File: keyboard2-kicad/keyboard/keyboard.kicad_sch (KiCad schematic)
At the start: 232 parts, among them J1 USB_C_Receptacle, J2 USB_BOOT, SW1 Esc, SW10 F9, SW100 Enter, SW11 F10, SW12 F11, SW13 F12, SW14 DEL, SW15 HOME, SW16 END, SW17 PGUP, SW18 PGDN, SW19 INS, SW2 F1, SW20 TILDE, SW21 1, SW22 2, SW23 3, SW24 4, SW25 5, SW26 6, SW27 7, SW28 8, SW29 9, SW3 F2, SW30 0, SW31 -, SW32 =, SW33 BKSP, SW34 Num, SW35 /, SW36 *, SW37 -, SW38 Tab, SW39 Q, SW4 F3, SW40 W, SW41 E, SW42 R, SW43 T, SW44 Y, SW45 U, SW46 I, SW47 O, SW48 P, SW49 [, SW5 F4, SW50 ], SW51 \, SW52 7, SW53 8, SW54 9, SW55 Caps, SW56 A, SW57 S, SW58 D, SW59 F, SW6 F5, SW60 G, SW61 H, SW62 J, SW63 K, SW64 L, SW65 ;, SW66 ", SW67 Enter, SW68 4, SW69 5, SW7 F6, SW70 6, SW71 +, SW72 Shift, SW73 Z, SW74 X, SW75 C, SW76 V, SW77 B, SW78 N, SW79 M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

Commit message: move images and finish schematic
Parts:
- removed J2: USB_BOOT, Connector_PinHeader_2.54mm:PinHeader_1x02_P2.54mm_Vertical, symbol Connector_Generic:Conn_01x02
- added D101, D102, D103, D104, D105, D106, D107, D108, D109, D110, D111, D112, D113, D114, D115, D116, D117, D118, D119, D120, D121, D122, D123, D124, D125, D126, D127, D128, D129, D130, D131, D132, D133, D134, D135, D136, D137, D138, D139, D140, D141, D142, D143, D144, D145, D146, D147, D148, D149, D150, D151, D152, D153, D154, D155, D156, D157, D158, D159, D160, D161, D162, D163, D164, D165, D166, D167, D168, D169, D170, D171, D172, D173, D174, D175, D176, D177, D178, D179, D180, D181, D182, D183, D184, D185, D186, D187, D188, D189, D190, D191, D192, D193, D194, D195, D196, D197, D198, D199, D200: LED, LED_SMD:LED_0603_1608Metric, symbol Device:LED
- added J3: Touchscreen, Connector_PinHeader_2.54mm:PinHeader_1x14_P2.54mm_Vertical, symbol Connector:Conn_01x14_Pin
- added J4: Jack-DC, DC-005:NINIGI_DC-005, symbol Connector:Jack-DC
- added M1, M10, M2, M3, M4, M5, M6, M7, M8, M9: Motor_Servo, Connector_PinHeader_2.54mm:PinHeader_1x03_P2.54mm_Vertical, symbol Motor:Motor_Servo
- added R10, R100, R101, R102, R103, R104, R105, R106, R107, R108, R11, R12, R13, R14, R15, R16, R17, R18, R19, R20, R21, R22, R23, R24, R25, R26, R27, R28, R29, R30, R31, R32, R33, R34, R35, R36, R37, R38, R39, R40, R41, R42, R43, R44, R45, R46, R47, R48, R49, R50, R51, R52, R53, R54, R55, R56, R57, R58, R59, R60, R61, R62, R63, R64, R65, R66, R67, R68, R69, R70, R71, R72, R73, R74, R75, R76, R77, R78, R79, R80, R81, R82, R83, R84, R85, R86, R87, R88, R89, R9, R90, R91, R92, R93, R94, R95, R96, R97, R98, R99: 680R, Resistor_SMD:R_0402_1005Metric, symbol Device:R
- added RV1: Slider 1, PG151101S11:SW_PG151101S11, symbol Device:R_Potentiometer
- added RV2: Slider 2, PG151101S11:SW_PG151101S11, symbol Device:R_Potentiometer
- added S1: USB BOOT, TS-1187A-B-A-B:SW_TS-1187A-B-A-B, symbol TS-1187A-B-A-B:TS-1187A-B-A-B
- added SW101: RotaryEncoder, symbol Device:RotaryEncoder
- added U7: IRLML6344TRPBF, IRLML6344TRPBF:SOT95P240X112-3N, symbol IRLML6344TRPBF:IRLML6344TRPBF
- C12, C13, C14, C3, C4, C5, C6, C7, C8, C9: footprint Capacitor_SMD:C_0603_1608Metric -> Capacitor_SMD:C_0402_1005Metric
- D1, D10, D11, D12, D13, D14, D15, D16, D17, D18, D19, D2, D20, D21, D22, D23, D24, D25, D26, D27, D28, D29, D3, D30, D31, D32, D33, D34, D35, D36, D37, D38, D39, D4, D40, D41, D42, D43, D44, D45, D46, D47, D48, D49, D5, D50, D51, D52, D53, D54, D55, D56, D57, D58, D59, D6, D60, D61, D62, D63, D64, D65, D66, D67, D68, D69, D7, D70, D71, D72, D73, D74, D75, D76, D77, D78, D79, D8, D80, D81, D82, D83, D84, D85, D86, D87, D88, D89, D9, D90, D91, D92, D93, D94, D95, D96, D97, D98, D99: footprint (none) -> Diode_SMD:D_SOD-323
- D100: footprint (none) -> LED_SMD:LED_0603_1608Metric
- J1: footprint (none) -> TYPE-C-31-M-12:HRO_TYPE-C-31-M-12
- R5, R6, R7, R8: footprint (none) -> Resistor_SMD:R_0402_1005Metric
- SW1, SW10, SW100, SW11, SW12, SW13, SW14, SW15, SW16, SW17, SW18, SW19, SW2, SW20, SW21, SW22, SW23, SW24, SW25, SW26, SW27, SW28, SW29, SW3, SW30, SW31, SW32, SW33, SW34, SW35, SW36, SW37, SW38, SW39, SW4, SW40, SW41, SW42, SW43, SW44, SW45, SW46, SW47, SW48, SW49, SW5, SW50, SW51, SW52, SW53, SW54, SW55, SW56, SW57, SW58, SW59, SW6, SW60, SW61, SW62, SW63, SW64, SW65, SW66, SW67, SW68, SW69, SW7, SW70, SW71, SW72, SW73, SW74, SW75, SW76, SW77, SW78, SW79, SW8, SW80, SW81, SW82, SW83, SW84, SW85, SW86, SW87, SW88, SW89, SW9, SW90, SW91, SW92, SW93, SW94, SW95, SW96, SW97, SW98, SW99: footprint (none) -> PG151101S11:SW_PG151101S11
- U3: footprint Package_SO:SOIC-8_5.23x5.23mm_P1.27mm -> W25Q128JVSIQ:SOIC127P790X216-8N
- U4: footprint ABM8-272-T3:ABM8-272-T3 -> ABM8:XTAL_ABM8-272-T3
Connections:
- net +3V3: now also J3.1 (Pin_1), J3.4 (Pin_4), RV1.1, RV2.1
- net GND: now also J3.2 (Pin_2), J4.2, M1.3 (-), M10.3 (-), M2.3 (-), M3.3 (-), M4.3 (-), M5.3 (-), M6.3 (-), M8.3 (-), M9.3 (-), RV1.3, RV2.3, S1.C, S1.D, SW101.C, U7.2 (S)
- net at R2.1: now also S1.A, S1.B
- net SERVO_7: now reaches U1.11 (GPIO8)
- net SERVO_7: now also M7.1 (PWM)
- net SERVO_8: now reaches U1.12 (GPIO9)
- net SERVO_8: now also M8.1 (PWM)
- net SERVO_9: now reaches U1.13 (GPIO10)
- net SERVO_9: now also M9.1 (PWM)
- net SERVO_10: now reaches U1.14 (GPIO11)
- net SERVO_10: now also M10.1 (PWM)
- net EA: now reaches U1.15 (GPIO12)
- net EA: now also SW101.A
- net EB: now reaches U1.16 (GPIO13)
- net EB: now also SW101.B
- net POT_1: now reaches U1.17 (GPIO14)
- net POT_1: now also RV1.2
- net POT_2: now reaches U1.18 (GPIO15)
- net POT_2: now also RV2.2
- net SPI_MISO: now reaches U1.27 (GPIO16)
- net SPI_MISO: now also J3.13 (Pin_13), J3.9 (Pin_9)
- net SPI_DISPLAY_CS: now reaches U1.28 (GPIO17)
- net SPI_DISPLAY_CS: now also J3.3 (Pin_3)
- net SPI_SCK: now reaches U1.29 (GPIO18)
- net SPI_SCK: now also J3.10 (Pin_10), J3.7 (Pin_7)
- net SPI_MOSI: now reaches U1.30 (GPIO19)
- net SPI_MOSI: now also J3.12 (Pin_12), J3.6 (Pin_6)
- net SPI_TOUCH_CS: now reaches U1.31 (GPIO20)
- net SPI_TOUCH_CS: now also J3.11 (Pin_11)
- net DISPLAY_DC: now reaches U1.32 (GPIO21)
- net DISPLAY_DC: now also J3.5 (Pin_5)
- net TOUCH_INT: now reaches U1.34 (GPIO22)
- net TOUCH_INT: now also J3.14 (Pin_14)
- net TOUCH_LED: now reaches U1.35 (GPIO23)
- net TOUCH_LED: now also J3.8 (Pin_8)
- net LED_PWM: now reaches U1.36 (GPIO24)
- net LED_PWM: now also U7.1 (G)
- net SERVO_1: now reaches U1.4 (GPIO2)
- net SERVO_1: now also M1.1 (PWM)
- net SERVO_2: now reaches U1.5 (GPIO3)
- net SERVO_2: now also M2.1 (PWM)
- net SERVO_3: now reaches U1.6 (GPIO4)
- net SERVO_3: now also M3.1 (PWM)
- net SERVO_4: now reaches U1.7 (GPIO5)
- net SERVO_4: now also M4.1 (PWM)
- net SERVO_5: now reaches U1.8 (GPIO6)
- net SERVO_5: now also M5.1 (PWM)
- net SERVO_6: now reaches U1.9 (GPIO7)
- net SERVO_6: now also M6.1 (PWM)
- new net: D128.1 (K), R36.1
- new net: R10.2, R100.2, R101.2, R102.2, R103.2, R104.2, R105.2, R106.2, R107.2, R108.2, R11.2, R12.2, R13.2, R14.2, R15.2, R16.2, R17.2, R18.2, R19.2, R20.2, R21.2, R22.2, R23.2, R24.2, R25.2, R26.2, R27.2, R28.2, R29.2, R30.2, R31.2, R32.2, R33.2, R34.2, R35.2, R36.2, R37.2, R38.2, R39.2, R40.2, R41.2, R42.2, R43.2, R44.2, R45.2, R46.2, R47.2, R48.2, R49.2, R50.2, R51.2, R52.2, R53.2, R54.2, R55.2, R56.2, R57.2, R58.2, R59.2, R60.2, R61.2, R62.2, R63.2, R64.2, R65.2, R66.2, R67.2, R68.2, R69.2, R70.2, R71.2, R72.2, R73.2, R74.2, R75.2, R76.2, R77.2, R78.2, R79.2, R80.2, R81.2, R82.2, R83.2, R84.2, R85.2, R86.2, R87.2, R88.2, R89.2, R9.2, R90.2, R91.2, R92.2, R93.2, R94.2, R95.2, R96.2, R97.2, R98.2, R99.2, U7.3 (D)
- new net: D199.1 (K), R107.1
- new net: D153.1 (K), R61.1
- new net: D174.1 (K), R82.1
- new net: D180.1 (K), R88.1
- new net: D109.1 (K), R17.1
- new net: D155.1 (K), R63.1
- new net: D178.1 (K), R86.1
- new net: D134.1 (K), R42.1
- new net: D151.1 (K), R59.1
- new net: D188.1 (K), R96.1
- new net: D136.1 (K), R44.1
- new net: D129.1 (K), R37.1
- new net: D149.1 (K), R57.1
- new net: D176.1 (K), R84.1
- new net: D200.1 (K), R108.1
- new net: D146.1 (K), R54.1
- new net: D181.1 (K), R89.1
- new net: D132.1 (K), R40.1
- new net: D114.1 (K), R22.1
- new net: D106.1 (K), R14.1
- new net: D138.1 (K), R46.1
- new net: D168.1 (K), R76.1
- new net: D182.1 (K), R90.1
- new net: D165.1 (K), R73.1
- new net: D187.1 (K), R95.1
- new net: D196.1 (K), R104.1
- new net: D194.1 (K), R102.1
- new net: D113.1 (K), R21.1
- new net: D177.1 (K), R85.1
- new net: D133.1 (K), R41.1
- new net: D152.1 (K), R60.1
- new net: D161.1 (K), R69.1
- new net: D175.1 (K), R83.1
- new net: D122.1 (K), R30.1
- new net: D157.1 (K), R65.1
- new net: D119.1 (K), R27.1
- new net: D104.1 (K), R12.1
- new net: D103.1 (K), R11.1
- new net: D121.1 (K), R29.1
- new net: D115.1 (K), R23.1
- new net: D142.1 (K), R50.1
- new net: D191.1 (K), R99.1
- new net: D112.1 (K), R20.1
- new net: D169.1 (K), R77.1
- new net: D172.1 (K), R80.1
- new net: D116.1 (K), R24.1
- new net: D164.1 (K), R72.1
- new net: D141.1 (K), R49.1
- new net: D148.1 (K), R56.1
- new net: D184.1 (K), R92.1
- new net: D193.1 (K), R101.1
- new net: D156.1 (K), R64.1
- new net: D102.1 (K), R10.1
- new net: D171.1 (K), R79.1
- new net: D118.1 (K), R26.1
- new net: D192.1 (K), R100.1
- new net: D162.1 (K), R70.1
- new net: D166.1 (K), R74.1
- new net: D111.1 (K), R19.1
- new net: D101.1 (K), R9.1
- new net: D110.1 (K), R18.1
- new net: D160.1 (K), R68.1
- new net: D163.1 (K), R71.1
- new net: D123.1 (K), R31.1
- new net: D127.1 (K), R35.1
- new net: D183.1 (K), R91.1
- new net: D120.1 (K), R28.1
- new net: D185.1 (K), R93.1
- new net: D131.1 (K), R39.1
- new net: D158.1 (K), R66.1
- new net: D130.1 (K), R38.1
- new net: D139.1 (K), R47.1
- new net: D125.1 (K), R33.1
- new net: D167.1 (K), R75.1
- new net: D147.1 (K), R55.1
- new net: D195.1 (K), R103.1
- new net: D143.1 (K), R51.1
- new net: D124.1 (K), R32.1
- new net: D154.1 (K), R62.1
- new net: D198.1 (K), R106.1
- new net: D144.1 (K), R52.1
- new net: D150.1 (K), R58.1
- new net: D190.1 (K), R98.1
- new net: D117.1 (K), R25.1
- new net: D170.1 (K), R78.1
- new net: D135.1 (K), R43.1
- new net: D189.1 (K), R97.1
- new net: D173.1 (K), R81.1
- new net: D140.1 (K), R48.1
- new net: D145.1 (K), R53.1
- new net: D197.1 (K), R105.1
- new net: D126.1 (K), R34.1
- new net: D186.1 (K), R94.1
- new net: D159.1 (K), R67.1
- new net: D107.1 (K), R15.1
- new net: D105.1 (K), R13.1
- new net: D137.1 (K), R45.1
- new net: D179.1 (K), R87.1
- new net: D108.1 (K), R16.1
- new net +5V: D101.2 (A), D102.2 (A), D103.2 (A), D104.2 (A), D105.2 (A), D106.2 (A), D107.2 (A), D108.2 (A), D109.2 (A), D110.2 (A), D111.2 (A), D112.2 (A), D113.2 (A), D114.2 (A), D115.2 (A), D116.2 (A), D117.2 (A), D118.2 (A), D119.2 (A), D120.2 (A), D121.2 (A), D122.2 (A), D123.2 (A), D124.2 (A), D125.2 (A), D126.2 (A), D127.2 (A), D128.2 (A), D129.2 (A), D130.2 (A), D131.2 (A), D132.2 (A), D133.2 (A), D134.2 (A), D135.2 (A), D136.2 (A), D137.2 (A), D138.2 (A), D139.2 (A), D140.2 (A), D141.2 (A), D142.2 (A), D143.2 (A), D144.2 (A), D145.2 (A), D146.2 (A), D147.2 (A), D148.2 (A), D149.2 (A), D150.2 (A), D151.2 (A), D152.2 (A), D153.2 (A), D154.2 (A), D155.2 (A), D156.2 (A), D157.2 (A), D158.2 (A), D159.2 (A), D160.2 (A), D161.2 (A), D162.2 (A), D163.2 (A), D164.2 (A), D165.2 (A), D166.2 (A), D167.2 (A), D168.2 (A), D169.2 (A), D170.2 (A), D171.2 (A), D172.2 (A), D173.2 (A), D174.2 (A), D175.2 (A), D176.2 (A), D177.2 (A), D178.2 (A), D179.2 (A), D180.2 (A), D181.2 (A), D182.2 (A), D183.2 (A), D184.2 (A), D185.2 (A), D186.2 (A), D187.2 (A), D188.2 (A), D189.2 (A), D190.2 (A), D191.2 (A), D192.2 (A), D193.2 (A), D194.2 (A), D195.2 (A), D196.2 (A), D197.2 (A), D198.2 (A), D199.2 (A), D200.2 (A), J4.1, M1.2 (+), M10.2 (+), M2.2 (+), M3.2 (+), M4.2 (+), M5.2 (+), M6.2 (+), M7.2 (+), M8.2 (+), M9.2 (+)
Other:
- note added: "CS"
- note added: "DC"
- note added: "GND"
- note added: "LED"
- note added: "MISO"
- note added: "MOSI"
- note added: "RESET"
- note added: "SCK"
- note added: "T_CLK"
- note added: "T_CS"
- note added: "T_DIN"
- note added: "T_DO"
- note added: "T_IRQ"
- note added: "VCC"

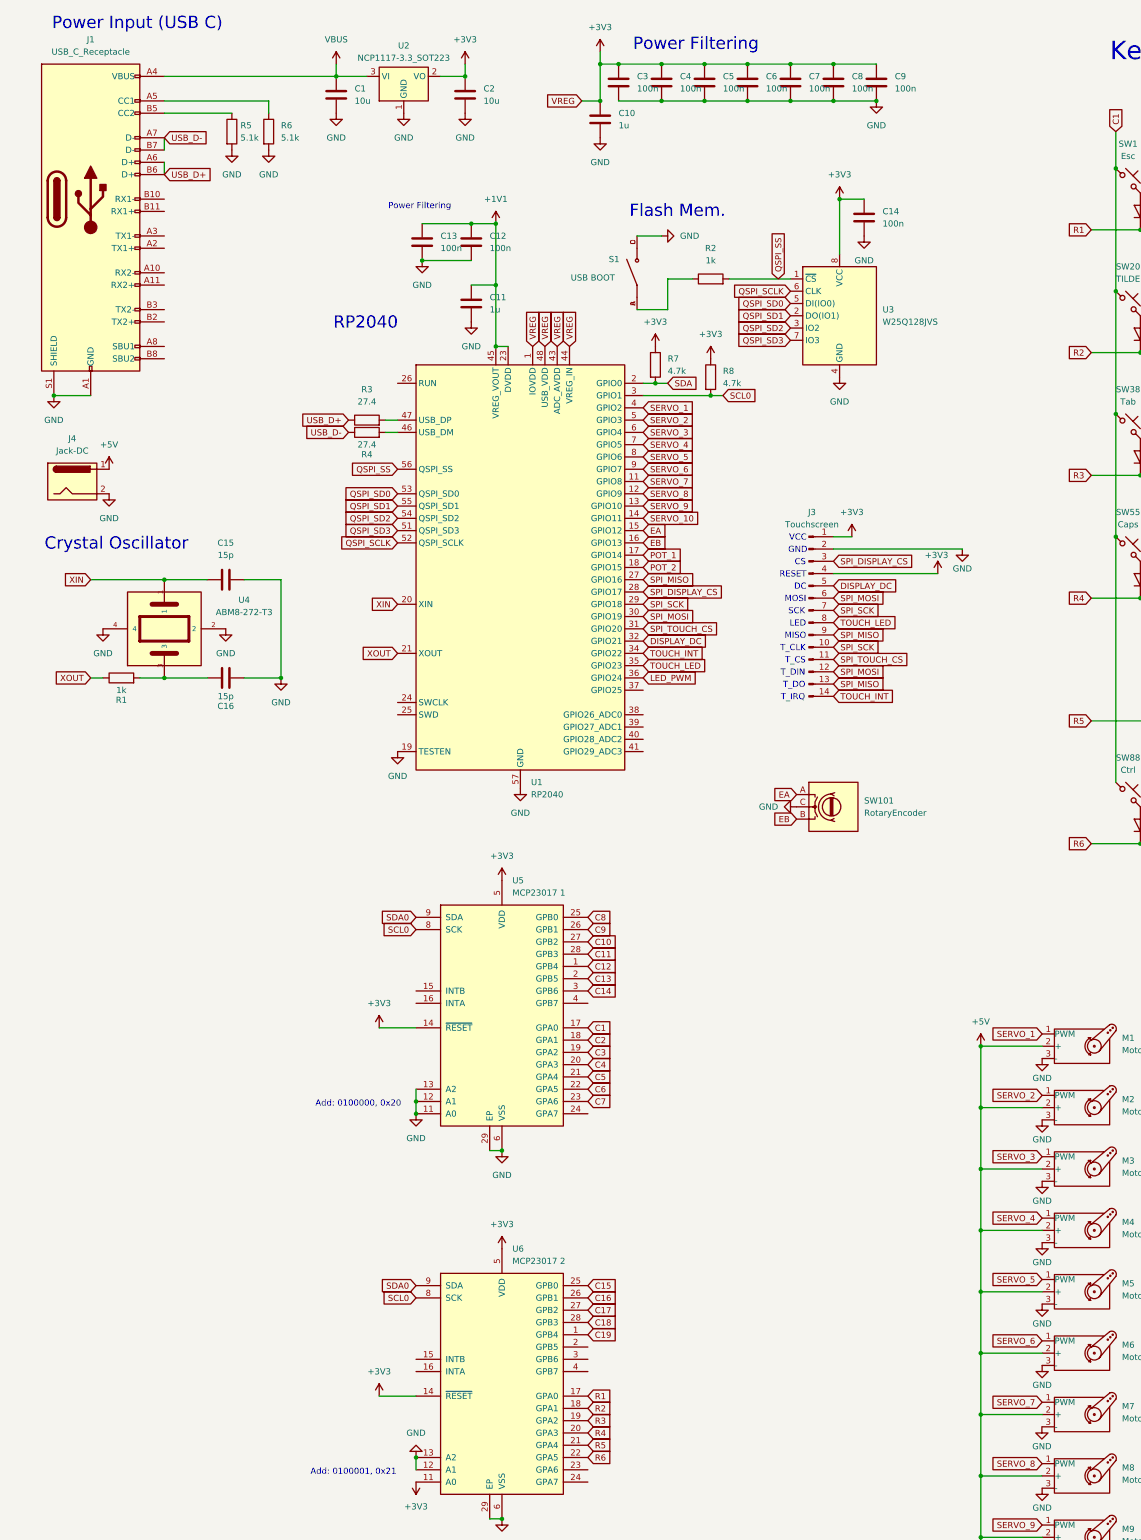
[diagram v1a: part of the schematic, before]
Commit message: keyb pcb finished w/ wrong switches
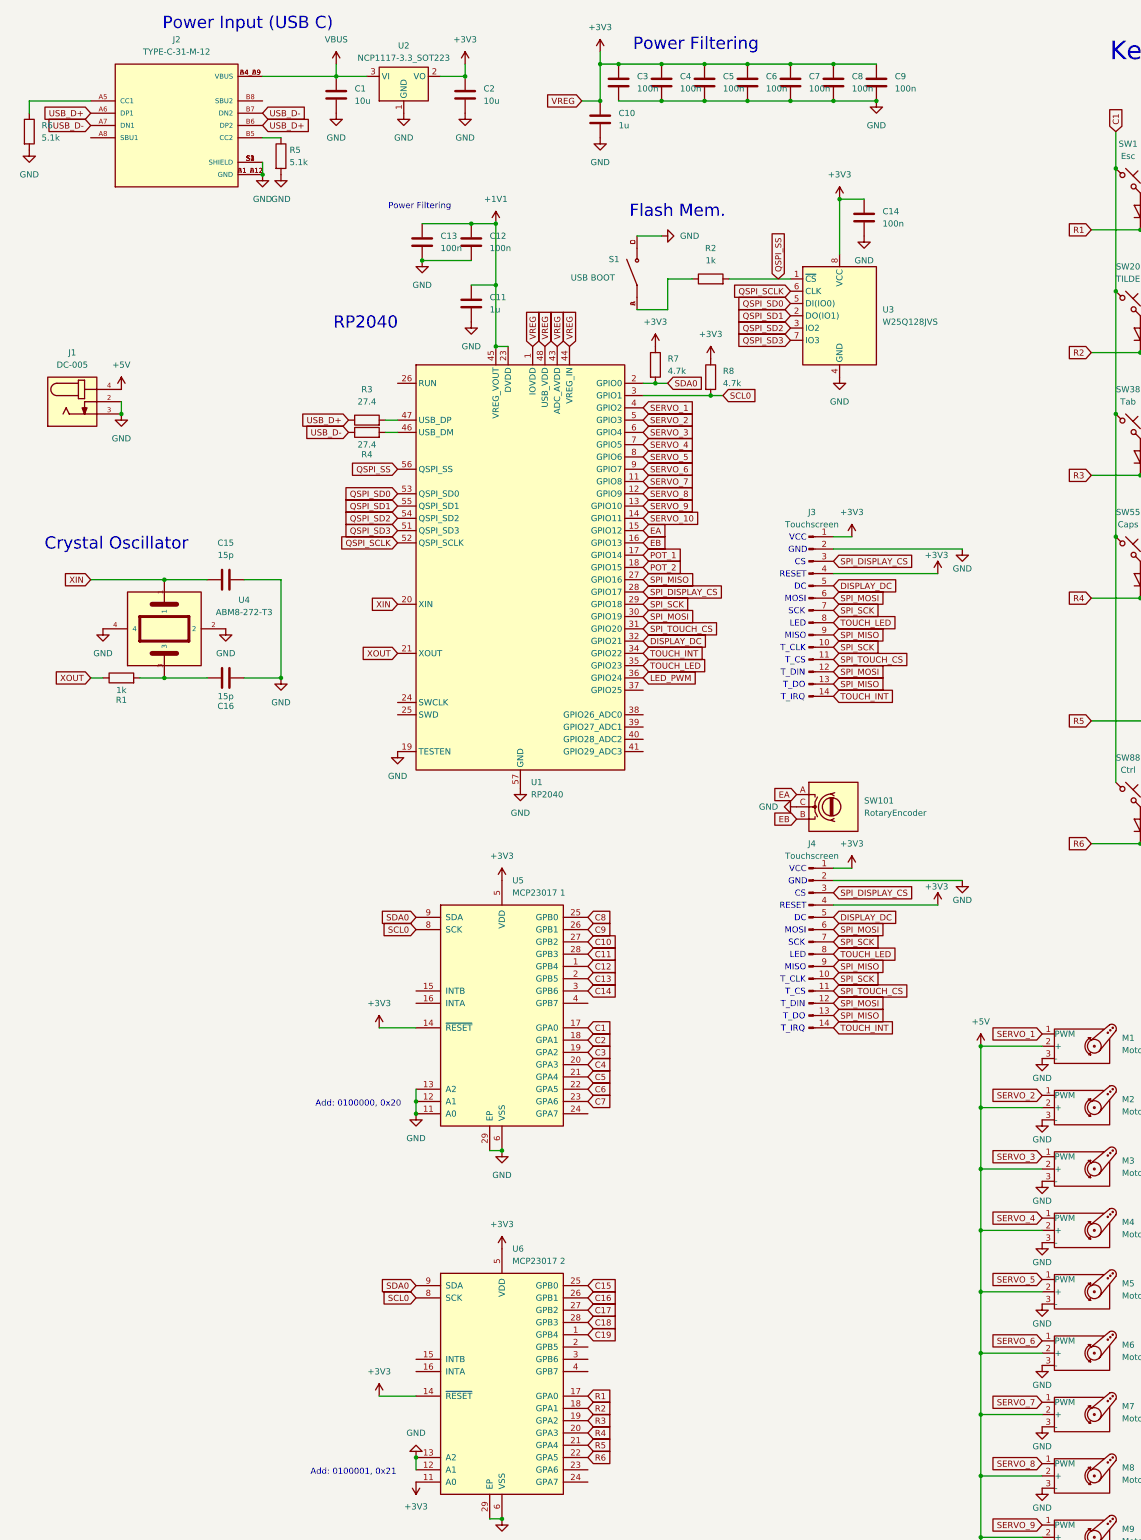
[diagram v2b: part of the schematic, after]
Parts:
- removed J1: USB_C_Receptacle, TYPE-C-31-M-12:HRO_TYPE-C-31-M-12, symbol Connector:USB_C_Receptacle
- removed J4: Jack-DC, DC-005:NINIGI_DC-005, symbol Connector:Jack-DC
- added J1: DC-005, DC-005:NINIGI_DC-005, symbol DC-005:DC-005
- added J2: TYPE-C-31-M-12, TYPE-C-31-M-12:HRO_TYPE-C-31-M-12, symbol TYPE-C-31-M-12:TYPE-C-31-M-12
- added J4: Touchscreen, Connector_PinHeader_2.54mm:PinHeader_1x14_P2.54mm_Vertical, symbol Connector:Conn_01x14_Pin
- D100: footprint LED_SMD:LED_0603_1608Metric -> Diode_SMD:D_SOD-323
- M1, M10, M2, M3, M4, M5, M6, M7, M8, M9: footprint Connector_PinHeader_2.54mm:PinHeader_1x03_P2.54mm_Vertical -> Connector_PinHeader_2.54mm:PinHeader_1x03_P2.54mm_Horizontal
- R1, R2, R3, R4: footprint Resistor_SMD:R_0603_1608Metric -> Resistor_SMD:R_0402_1005Metric
- RV1, RV2: footprint PG151101S11:SW_PG151101S11 -> (none)
- SW1, SW10, SW11, SW12, SW13, SW14, SW15, SW16, SW17, SW18, SW19, SW2, SW20, SW21, SW22, SW23, SW24, SW25, SW26, SW27, SW28, SW29, SW3, SW30, SW31, SW32, SW34, SW35, SW36, SW37, SW39, SW4, SW40, SW41, SW42, SW43, SW44, SW45, SW46, SW47, SW48, SW49, SW5, SW50, SW52, SW53, SW54, SW56, SW57, SW58, SW59, SW6, SW60, SW61, SW62, SW63, SW64, SW65, SW66, SW68, SW69, SW7, SW70, SW73, SW74, SW75, SW76, SW77, SW78, SW79, SW8, SW80, SW81, SW82, SW84, SW85, SW86, SW87, SW9, SW92, SW93, SW94, SW95, SW96, SW97, SW98, SW99: footprint PG151101S11:SW_PG151101S11 -> MX_Hotswap:MX-Hotswap-1U
- SW100, SW71: footprint PG151101S11:SW_PG151101S11 -> MX_Hotswap:MX-Hotswap-2U-Vertical
- SW33: footprint PG151101S11:SW_PG151101S11 -> MX_Hotswap:MX-Hotswap-2U
- SW38, SW51: footprint PG151101S11:SW_PG151101S11 -> MX_Hotswap:MX-Hotswap-1.5U
- SW55, SW83: footprint PG151101S11:SW_PG151101S11 -> MX_Hotswap:MX-Hotswap-1.75U
- SW67, SW72: footprint PG151101S11:SW_PG151101S11 -> MX_Hotswap:MX-Hotswap-2.25U
- SW88, SW89, SW90: footprint PG151101S11:SW_PG151101S11 -> MX_Hotswap:MX-Hotswap-1.25U
- SW91: footprint PG151101S11:SW_PG151101S11 -> MX_Hotswap:MX-Hotswap-6.25U
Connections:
- net SDA is gone; now on net SDA0: R7.2, U1.2 (GPIO0)
- net +3V3: now also J4.1 (Pin_1), J4.4 (Pin_4)
- net +5V: now also J1.4
- net DISPLAY_DC: now also J4.5 (Pin_5)
- net GND: now also M7.3 (-), J1.2, J1.3, J2.A1_B12 (GND), J2.B1_A12 (GND), J2.S1 (SHIELD), J2.S2 (SHIELD), J2.S3 (SHIELD), J2.S4 (SHIELD), J4.2 (Pin_2)
- net SPI_DISPLAY_CS: now also J4.3 (Pin_3)
- net SPI_MISO: now also J4.13 (Pin_13), J4.9 (Pin_9)
- net SPI_MOSI: now also J4.12 (Pin_12), J4.6 (Pin_6)
- net SPI_SCK: now also J4.10 (Pin_10), J4.7 (Pin_7)
- net SPI_TOUCH_CS: now also J4.11 (Pin_11)
- net TOUCH_INT: now also J4.14 (Pin_14)
- net TOUCH_LED: now also J4.8 (Pin_8)
- net USB_D+: now also J2.A6 (DP1), J2.B6 (DP2)
- net USB_D-: now also J2.A7 (DN1), J2.B7 (DN2)
- net VBUS: now also J2.A4_B9 (VBUS), J2.B4_A9 (VBUS)
- net at R6.1: now also J2.A5 (CC1)
- net at R5.1: now also J2.B5 (CC2)
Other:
- moved on the sheet: R5, R6

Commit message: yeah, just everything
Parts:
- removed RV1: Slider 1, symbol Device:R_Potentiometer
- removed RV2: Slider 2, symbol Device:R_Potentiometer
- added R109, R110: PTA3043-2010CIB103, PTA3043-2010CIB103:TRIM_PTA3043-2010CIB103, symbol PTA3043-2010CIB103:PTA3043-2010CIB103
- SW101: footprint (none) -> EC10E1220501:TRIM_EC10E1220501
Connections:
- net +3V3: now also R109.3, R110.3
- net EA: now also U6.2 (GPB5); no longer U1.15 (GPIO12)
- net EB: now also U6.3 (GPB6); no longer U1.16 (GPIO13)
- net GND: now also R109.1, R109.SH1 (SHIELD), R109.SH2 (SHIELD), R109.SH3 (SHIELD), R109.SH4 (SHIELD), R110.1, R110.SH1 (SHIELD), R110.SH2 (SHIELD), R110.SH3 (SHIELD), R110.SH4 (SHIELD)
- net POT_1: now also U6.4 (GPB7), R110.2; no longer U1.17 (GPIO14)
- net POT_2: now also U6.23 (GPA6), R109.2; no longer U1.18 (GPIO15)
